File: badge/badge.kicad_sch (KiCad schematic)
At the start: 25 parts, among them SW1 SW_Push, Y2 1.843

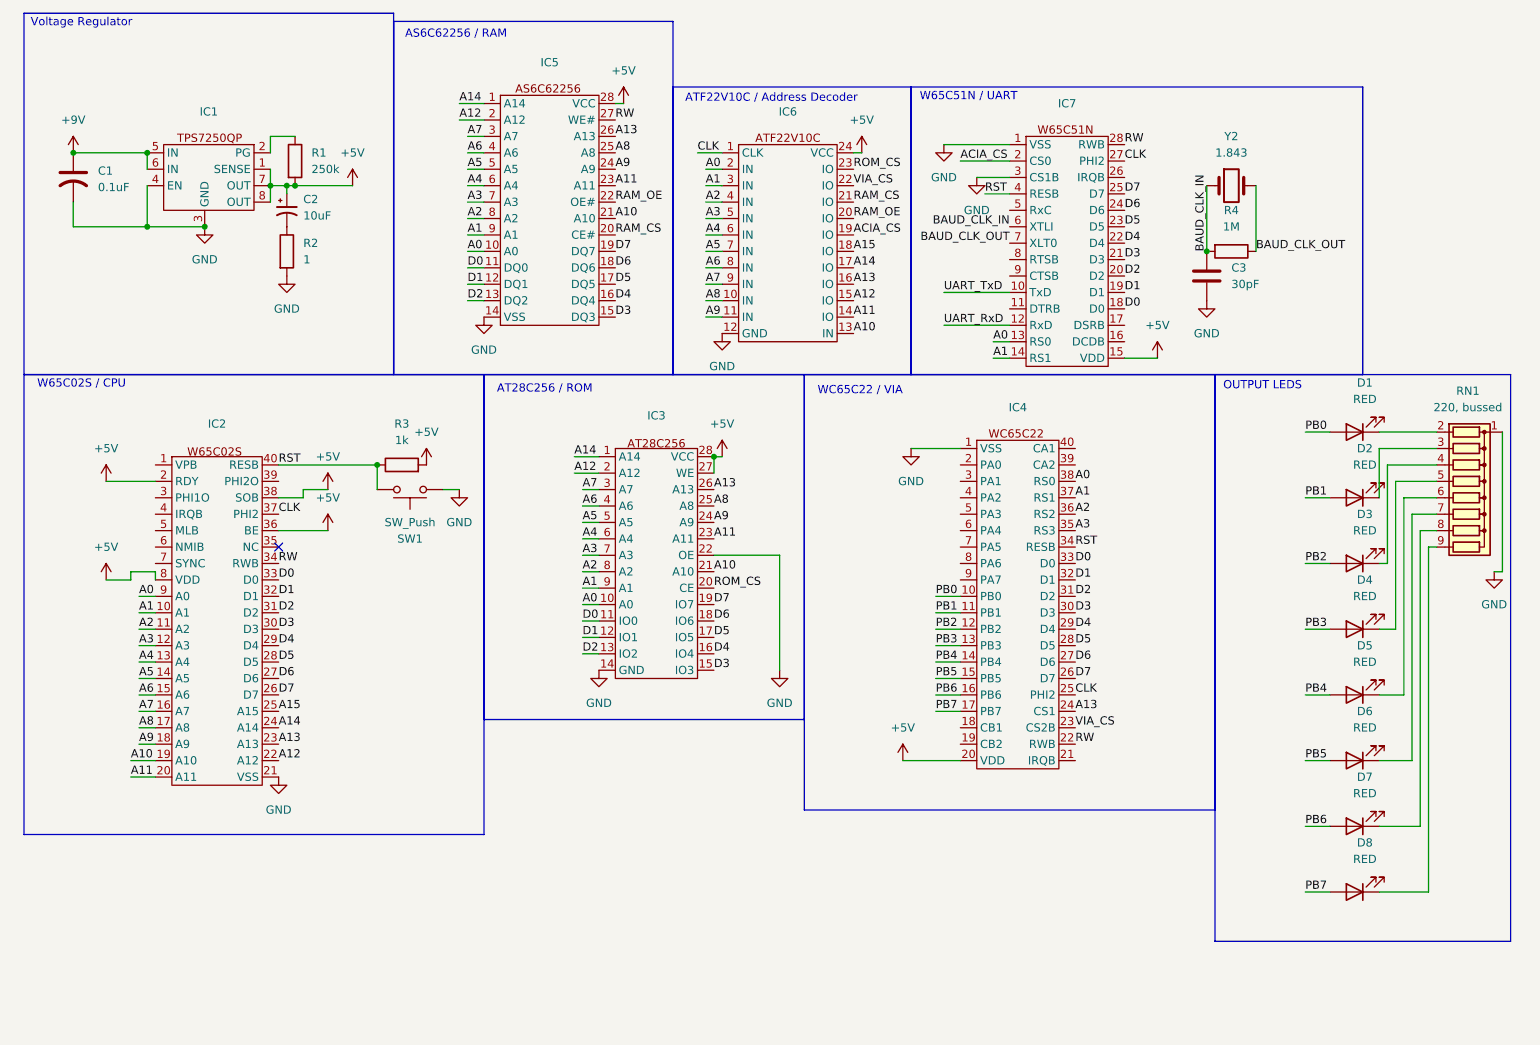
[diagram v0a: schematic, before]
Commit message: Add clock and some notes about a USB to UART adapter
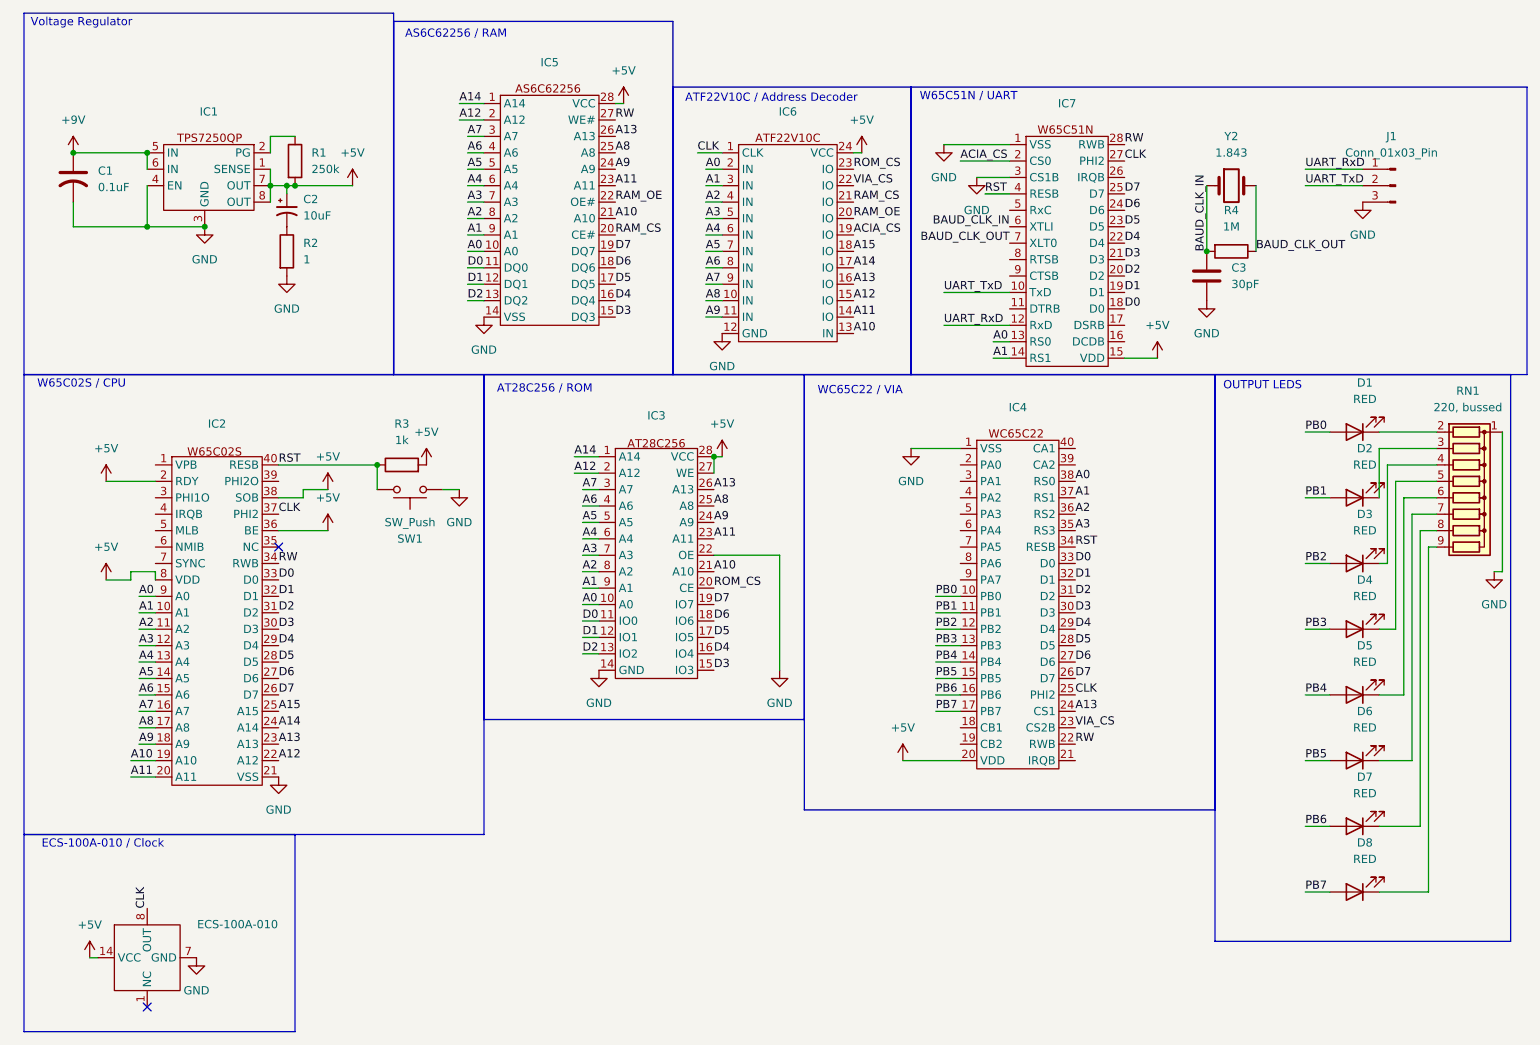
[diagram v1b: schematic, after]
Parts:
- added ECS-100A-010: ~, symbol 6502ConferenceBadge:ECS-100A-010
- added J1: Conn_01x03_Pin, symbol Connector:Conn_01x03_Pin
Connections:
- net +5V: now also ECS-100A-010.14 (VCC)
- net CLK: now also ECS-100A-010.8 (OUT)
- net GND: now also ECS-100A-010.7 (GND), J1.3 (Pin_3)
- net UART_RxD: now also J1.1 (Pin_1)
- net UART_TxD: now also J1.2 (Pin_2)
- no-connect marks 1 -> 2
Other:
- note added: "ECS-100A-010 / Clock"

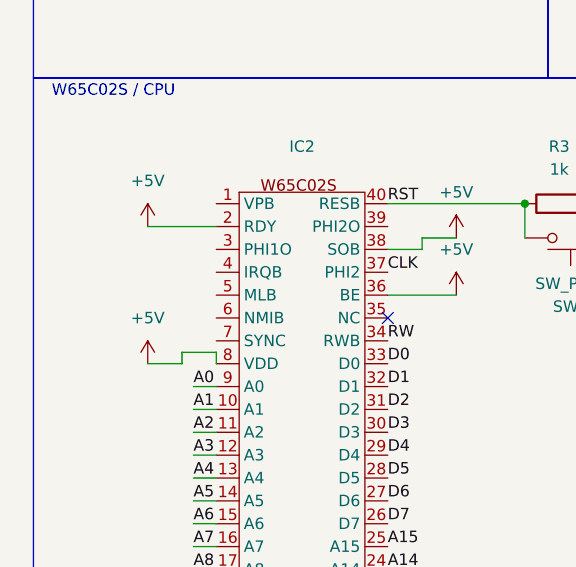
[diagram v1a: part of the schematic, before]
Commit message: Add a few missing power connections, fix an image link and add a schematic plot
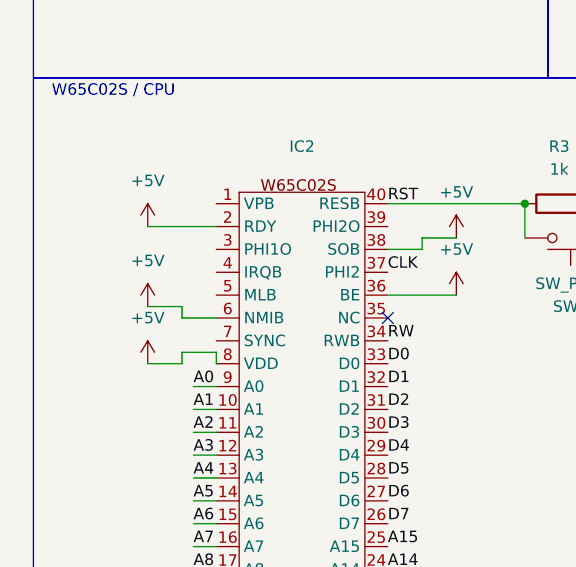
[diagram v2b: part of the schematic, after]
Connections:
- net +5V: now also IC2.6 (NMIB)
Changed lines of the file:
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@@
 	(wire
 		(pts
+			(xy 27.94 93.98) (xy 27.94 92.71)
+		)
+		(stroke
+			(width 0)
+			(type default)
+		)
+	)
+	(wire
+		(pts
 			(xy 27.94 127) (xy 31.75 127)
 		)
@@
 	(wire
 		(pts
+			(xy 27.94 92.71) (xy 24.13 92.71)
+		)
+		(stroke
+			(width 0)
+			(type default)
+		)
+	)
+	(wire
+		(pts
 			(xy 153.67 31.75) (xy 163.83 31.75)
 		)
@@
 	(wire
 		(pts
+			(xy 31.75 93.98) (xy 27.94 93.98)
+		)
+		(stroke
+			(width 0)
+			(type default)
+		)
+	)
+	(wire
+		(pts
 			(xy 186.69 64.77) (xy 181.61 64.77)
 		)
@@
 					(unit 1)
 				)
+			)
+		)
+	)
+	(symbol
+		(lib_id "power:+5V")
+		(at 24.13 92.71 0)
+		(unit 1)
+		(exclude_from_sim no)
+		(in_bom yes)
+		(on_board yes)
+		(dnp no)
+		(fields_autoplaced yes)
+		(property "Reference" "#PWR030"
+			(at 24.13 96.52 0)
+			(effects
+				(font
+					(size 1.27 1.27)
+				)
+				(hide yes)
+			)
+		)
+		(property "Value" "+5V"
+			(at 24.13 87.63 0)
+			(effects
+				(font
+					(size 1.27 1.27)
+				)
+			)
+		)
+		(property "Footprint" ""
+			(at 24.13 92.71 0)
+			(effects
+				(font
+					(size 1.27 1.27)
+				)
+				(hide yes)
+			)
+		)
+		(property "Datasheet" ""
+			(at 24.13 92.71 0)
+			(effects
+				(font
+					(size 1.27 1.27)
+				)
+				(hide yes)
+			)
+		)
+		(property "Description" "Power symbol creates a global label with name \"+5V\""
+			(at 24.13 92.71 0)
+			(effects
+				(font
+					(size 1.27 1.27)
+				)
+				(hide yes)
+			)
+		)
+		(pin "1"
+		)
+		(instances
+			(project "badge"
+				(path "/fa0ed09a-51e0-455c-851f-6bdd2d2f2109"
+					(reference "#PWR030")
+					(unit 1)
+				)
